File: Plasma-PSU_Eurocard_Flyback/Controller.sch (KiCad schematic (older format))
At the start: 4 parts

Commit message: Block diagram, Connectivity, Isolation
- First page reservered for block diagram
- Connectors moved to separate sheet
- Opto-isolators for signal inputs on HV board
- Fuse added to SMPS
- Pinheader for Arduino pin-out, UART, I2C, SPI
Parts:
- removed J?: I2C, symbol Connector_Generic:Conn_01x02
- removed SW?: SW_RESET, symbol Switch:SW_Push
- added J?: Arduino_Pinout_01-15, symbol Connector_Generic:Conn_01x15
- added J?: Arduino_Pinout_16-30, symbol Connector_Generic:Conn_01x15
- added J?: SPI, symbol Connector_Generic:Conn_01x06
- added J?: I2C, symbol Connector_Generic:Conn_02x04_Odd_Even
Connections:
- net labels added: D13_16, RES_3
- wire segments 14 -> 84
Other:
- note added: "I2C\n\nSCL\nSDA\n+5V\nGND"
- note added: "SPI\n\nSCK\nMISO\nMOSI\nCS\n+5V\nGND"
- note removed: "SDA\nSCL"
- moved on the sheet: J?

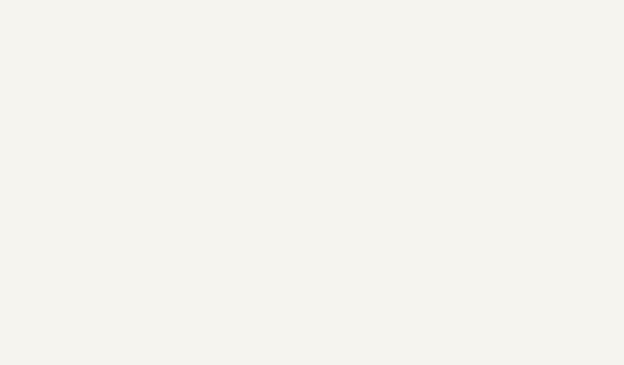
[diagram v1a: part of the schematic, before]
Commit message: STM6600 power-up included
An STM6600 IC is now used to enable stand-by and touch-button operation
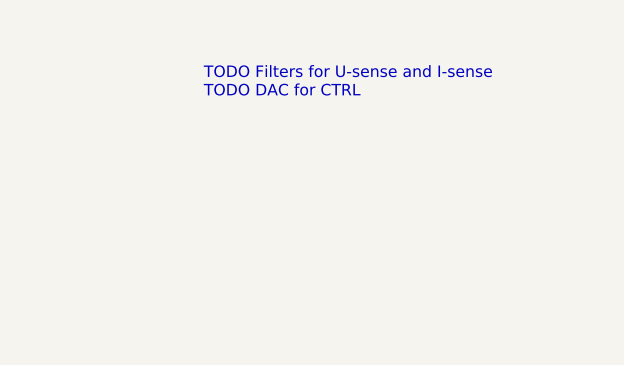
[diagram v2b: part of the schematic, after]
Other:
- note added: "TODO Filters for U-sense and I-sense\nTODO DAC for CTRL"
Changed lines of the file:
@@
 	4150 3500 4150 4400
 Connection ~ 4900 3500
+Text Notes 9000 1000 0    50   ~ 0
+TODO Filters for U-sense and I-sense\nTODO DAC for CTRL
 $EndSCHEMATC

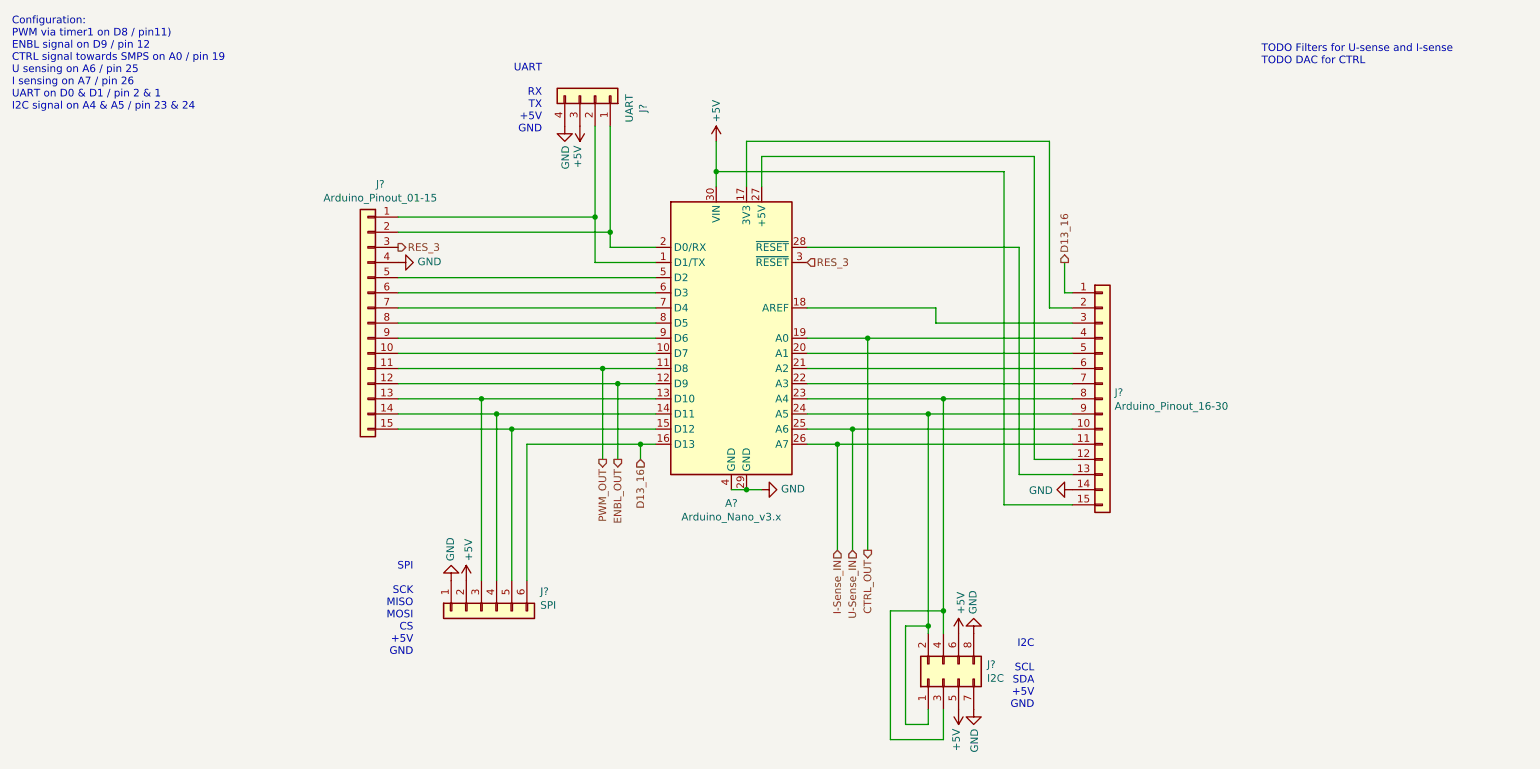
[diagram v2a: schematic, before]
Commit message: Filters for sense signals
- RC filters on U-sense and I-sense included
- Block diagram refined
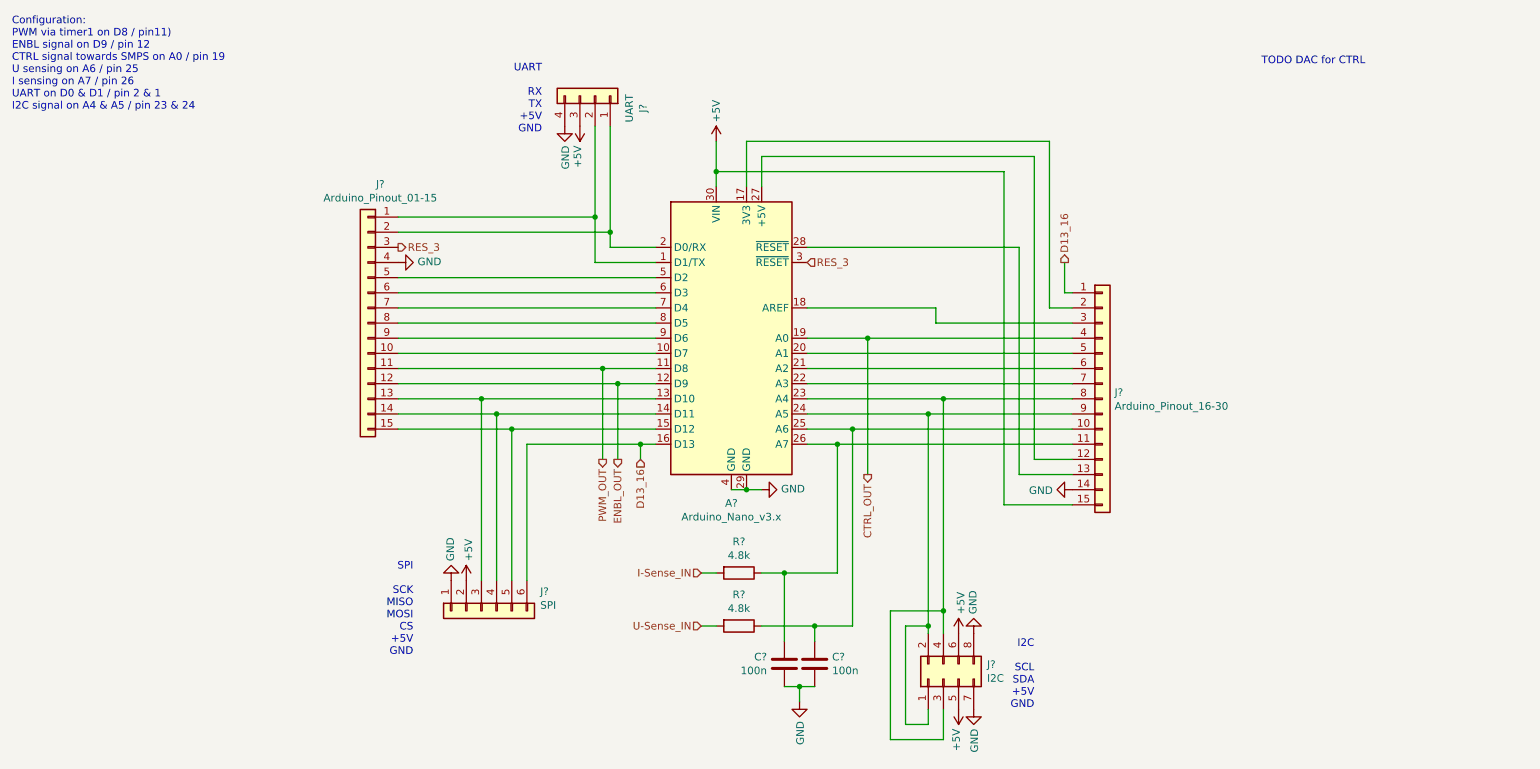
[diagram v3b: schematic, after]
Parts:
- added C? (x2): 100n, symbol Device:C
- added R? (x2): 4.8k, symbol Device:R
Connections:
- net GND: now also C?.1, C?.2
- net I-Sense_IN: now also R?.2; no longer A?.26 (A7), J?.11 (Pin_11)
- net U-Sense_IN: now also R?.2; no longer A?.25 (A6), J?.10 (Pin_10)
- new net: A?.25 (A6), C?.1, J?.10 (Pin_10), R?.1
- new net: A?.26 (A7), C?.2, J?.11 (Pin_11), R?.1
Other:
- note added: "TODO DAC for CTRL"
- note removed: "TODO Filters for U-sense and I-sense\nTODO DAC for CTRL"
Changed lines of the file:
@@
 Sheet 3 5
 Title "Plasma-PSU_Eurocard_Flyback"
-Date "2020-04-07"
-Rev "0.0.3"
+Date "2020-04-08"
+Rev "0.0.4"
 Comp "University of Ljubljana"
 Comment1 "Biotechnical faculty"
@@
 	1    0    0    -1
 $EndComp
-Text HLabel 6400 4200 3    50   Output ~ 0
+Text HLabel 6400 3700 3    50   Output ~ 0
 CTRL_OUT
 Text HLabel 4750 3600 3    50   Output ~ 0
 ENBL_OUT
-Text HLabel 6200 4200 3    50   Input ~ 0
+Text HLabel 5300 4350 0    50   Input ~ 0
 I-Sense_IN
 Text HLabel 4650 3600 3    50   Output ~ 0
 PWM_OUT
-Text HLabel 6300 4200 3    50   Input ~ 0
+Text HLabel 5300 4700 0    50   Input ~ 0
 U-Sense_IN
 $Comp
@@
 $EndComp
 Wire Wire Line
-	6200 4200 6200 3500
-Wire Wire Line
 	6000 3500 6200 3500
 Wire Wire Line
-	6300 4200 6300 3400
-Wire Wire Line
 	6000 3400 6300 3400
-Wire Wire Line
-	6400 4200 6400 2800
 Wire Wire Line
 	6000 2800 6400 2800
@@
 Connection ~ 4900 3500
 Text Notes 9000 1000 0    50   ~ 0
-TODO Filters for U-sense and I-sense\nTODO DAC for CTRL
+TODO DAC for CTRL
+Wire Wire Line
+	6400 3700 6400 2800
+$Comp
+L Device:R R?
+U 1 1 5E90D904
+P 5550 4350
+F 0 "R?" V 5343 4350 50  0000 C CNN
+F 1 "4.8k" V 5434 4350 50  0000 C CNN
+F 2 "" V 5480 4350 50  0001 C CNN
+F 3 "~" H 5550 4350 50  0001 C CNN
+	1    5550 4350
+	0    1    1    0
+$EndComp
+$Comp
+L Device:R R?
+U 1 1 5E90DE41
+P 5550 4700
+F 0 "R?" V 5343 4700 50  0000 C CNN
+F 1 "4.8k" V 5434 4700 50  0000 C CNN
+F 2 "" V 5480 4700 50  0001 C CNN
+F 3 "~" H 5550 4700 50  0001 C CNN
+	1    5550 4700
+	0    1    1    0
+$EndComp
+Wire Wire Line
+	5400 4350 5300 4350
+Wire Wire Line
+	5300 4700 5400 4700
+Wire Wire Line
+	6200 3500 6200 4350
+Wire Wire Line
+	6300 3400 6300 4700
+$Comp
+L Device:C C?
+U 1 1 5E9180BC
+P 5850 4950
+F 0 "C?" H 5735 4904 50  0000 R CNN
+F 1 "100n" H 5735 4995 50  0000 R CNN
+F 2 "" H 5888 4800 50  0001 C CNN
+F 3 "~" H 5850 4950 50  0001 C CNN
+	1    5850 4950
+	1    0    0    1
+$EndComp
+$Comp
+L Device:C C?
+U 1 1 5E9189A9
+P 6050 4950
+F 0 "C?" H 6165 4996 50  0000 L CNN
+F 1 "100n" H 6165 4905 50  0000 L CNN
+F 2 "" H 6088 4800 50  0001 C CNN
+F 3 "~" H 6050 4950 50  0001 C CNN
+	1    6050 4950
+	1    0    0    -1
+$EndComp
+Wire Wire Line
+	5700 4700 6050 4700
+Wire Wire Line
+	5700 4350 5850 4350
+Wire Wire Line
+	5850 4800 5850 4350
+Wire Wire Line
+	6050 4800 6050 4700
+$Comp
+L power:GND #PWR?
+U 1 1 5E92882A
+P 5950 5200
+F 0 "#PWR?" H 5950 4950 50  0001 C CNN
+F 1 "GND" V 5955 5072 50  0000 R CNN
+F 2 "" H 5950 5200 50  0001 C CNN
+F 3 "" H 5950 5200 50  0001 C CNN
+	1    5950 5200
+	1    0    0    -1
+$EndComp
+Wire Wire Line
+	5850 5100 5950 5100
+Wire Wire Line
+	5950 5200 5950 5100
+Connection ~ 5950 5100
+Wire Wire Line
+	5950 5100 6050 5100
+Connection ~ 5850 4350
+Connection ~ 6050 4700
+Wire Wire Line
+	5850 4350 6200 4350
+Wire Wire Line
+	6050 4700 6300 4700
 $EndSCHEMATC

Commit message: DAC sets U_out
DAC converter in SMPS sheet sets boost modules output voltage.
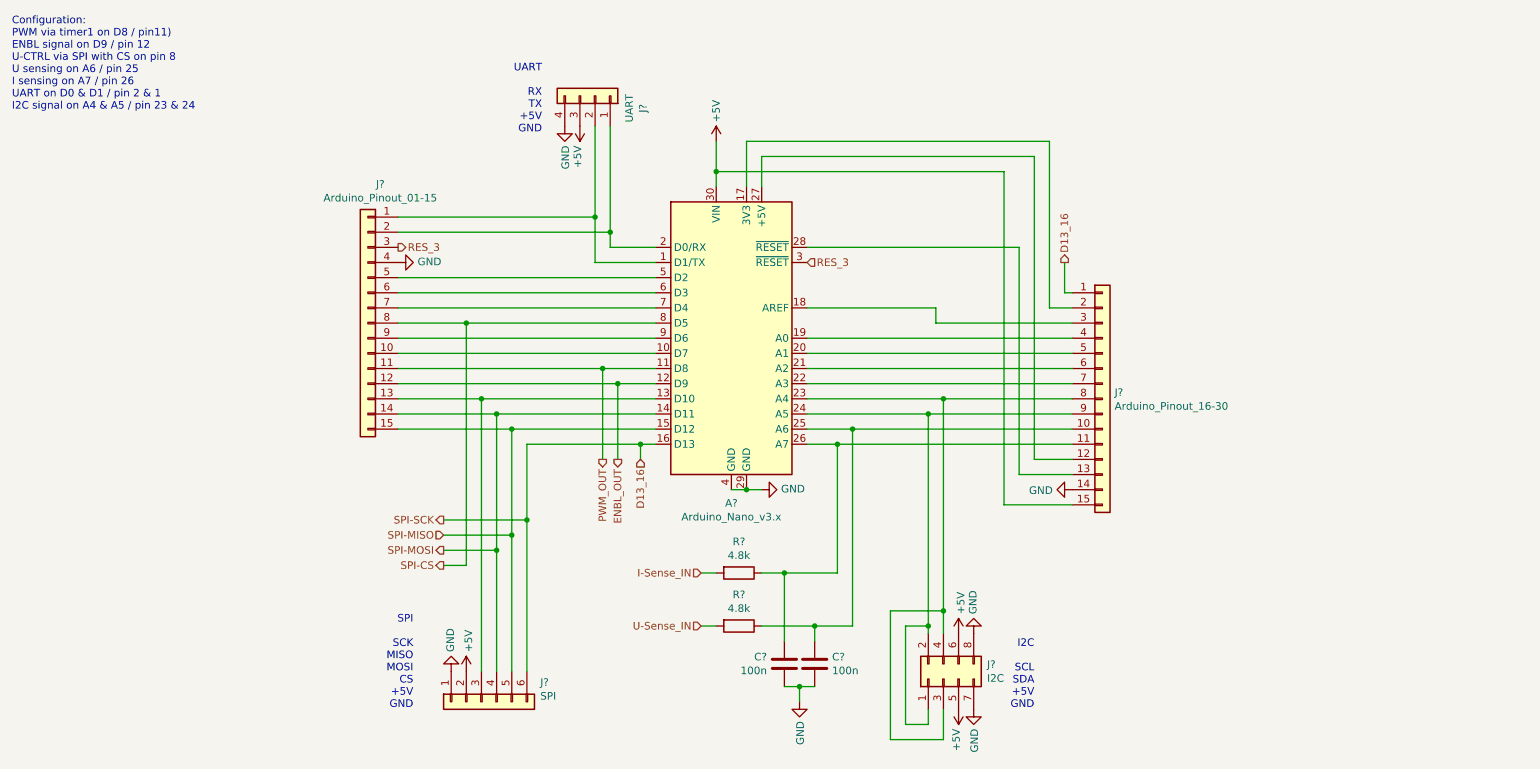
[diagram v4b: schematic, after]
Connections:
- net SPI-MOSI: now reaches A?.14 (D11), J?.14 (Pin_14), J?.4 (Pin_4)
- net SPI-MISO: now reaches A?.15 (D12), J?.15 (Pin_15), J?.5 (Pin_5)
- net SPI-CS: now reaches A?.8 (D5), J?.8 (Pin_8)
- net CTRL_OUT: no longer names the net of A?.19 (A0), J?.4 (Pin_4)
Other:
- note added: "Configuration:\nPWM via timer1 on D8 / pin11)\nENBL signal on D9 / pin 12\nU-CTRL via SPI with CS on pin 8\nU sensing on A6 / pin 25\nI sensing on A7 / pin 26\nUART on D0 & D1 / pin 2 & 1\nI2C signal on A4 & A5 / pin 23 & 24"
- note removed: "Configuration:\nPWM via timer1 on D8 / pin11)\nENBL signal on D9 / pin 12\nCTRL signal towards SMPS on A0 / pin 19\nU sensing on A6 / pin 25\nI sensing on A7 / pin 26\nUART on D0 & D1 / pin 2 & 1\nI2C signal on A4 & A5 / pin 23 & 24"
- note removed: "TODO DAC for CTRL"
- moved on the sheet: J?
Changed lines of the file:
@@
 	1    0    0    -1
 $EndComp
-Text HLabel 6400 3700 3    50   Output ~ 0
-CTRL_OUT
 Text HLabel 4750 3600 3    50   Output ~ 0
 ENBL_OUT
@@
 	5600 3800 5500 3800
 Text Notes 750  1300 0    50   ~ 0
-Configuration:\nPWM via timer1 on D8 / pin11)\nENBL signal on D9 / pin 12\nCTRL signal towards SMPS on A0 / pin 19\nU sensing on A6 / pin 25\nI sensing on A7 / pin 26\nUART on D0 & D1 / pin 2 & 1\nI2C signal on A4 & A5 / pin 23 & 24
+Configuration:\nPWM via timer1 on D8 / pin11)\nENBL signal on D9 / pin 12\nU-CTRL via SPI with CS on pin 8\nU sensing on A6 / pin 25\nI sensing on A7 / pin 26\nUART on D0 & D1 / pin 2 & 1\nI2C signal on A4 & A5 / pin 23 & 24
 $Comp
 L Connector_Generic:Conn_01x04 J?
@@
 Wire Wire Line
 	6000 3400 6300 3400
-Wire Wire Line
-	6000 2800 6400 2800
 Text HLabel 4900 3600 3    50   Input ~ 0
 D13_16
@@
 Wire Wire Line
 	6000 3000 7750 3000
-Wire Wire Line
-	6400 2800 7750 2800
-Connection ~ 6400 2800
 Wire Wire Line
 	6850 2700 7750 2700
@@
 Wire Wire Line
 	7500 1600 7500 3600
-$Comp
-L Connector_Generic:Conn_01x06 J?
-U 1 1 5EA74613
-P 3850 4600
-F 0 "J?" V 3722 4212 50  0000 R CNN
-F 1 "SPI" V 3813 4212 50  0000 R CNN
-F 2 "" H 3850 4600 50  0001 C CNN
-F 3 "~" H 3850 4600 50  0001 C CNN
-	1    3850 4600
-	0    -1   1    0
-$EndComp
 Wire Wire Line
 	4700 1400 4700 2100
@@
 	3300 2600 5000 2600
 Wire Wire Line
-	3300 2700 5000 2700
-Wire Wire Line
 	3300 2800 5000 2800
 Wire Wire Line
@@
 	3300 3100 4750 3100
 Connection ~ 4750 3100
-Wire Wire Line
-	3300 3200 3850 3200
-$Comp
-L power:GND #PWR?
-U 1 1 5EA92261
-P 3650 4400
-F 0 "#PWR?" H 3650 4150 50  0001 C CNN
-F 1 "GND" V 3655 4272 50  0000 R CNN
-F 2 "" H 3650 4400 50  0001 C CNN
-F 3 "" H 3650 4400 50  0001 C CNN
-	1    3650 4400
-	-1   0    0    1
-$EndComp
-$Comp
-L power:+5V #PWR?
-U 1 1 5EA927CA
-P 3750 4400
-F 0 "#PWR?" H 3750 4250 50  0001 C CNN
-F 1 "+5V" V 3765 4528 50  0000 L CNN
-F 2 "" H 3750 4400 50  0001 C CNN
-F 3 "" H 3750 4400 50  0001 C CNN
-	1    3750 4400
-	1    0    0    -1
-$EndComp
 Text Notes 7500 5250 2    50   ~ 0
 I2C\n\nSCL\nSDA\n+5V\nGND
@@
 	1    0    0    -1
 $EndComp
-Text Notes 3400 4900 2    50   ~ 0
-SPI\n\nSCK\nMISO\nMOSI\nCS\n+5V\nGND
-Wire Wire Line
-	3850 4400 3850 3200
-Connection ~ 3850 3200
-Wire Wire Line
-	3850 3200 5000 3200
-Wire Wire Line
-	3300 3400 4050 3400
-Wire Wire Line
-	3300 3300 3950 3300
-Wire Wire Line
-	3950 4400 3950 3300
-Connection ~ 3950 3300
-Wire Wire Line
-	3950 3300 5000 3300
-Wire Wire Line
-	4050 4400 4050 3400
-Connection ~ 4050 3400
-Wire Wire Line
-	4050 3400 5000 3400
-Wire Wire Line
-	4900 3500 4150 3500
-Wire Wire Line
-	4150 3500 4150 4400
 Connection ~ 4900 3500
-Text Notes 9000 1000 0    50   ~ 0
-TODO DAC for CTRL
-Wire Wire Line
-	6400 3700 6400 2800
 $Comp
 L Device:R R?
@@
 Wire Wire Line
 	6050 4700 6300 4700
+Wire Wire Line
+	4900 3500 4150 3500
+Connection ~ 4050 3400
+Connection ~ 3950 3300
+Wire Wire Line
+	3950 3300 5000 3300
+Wire Wire Line
+	3300 3300 3950 3300
+Wire Wire Line
+	4050 3400 5000 3400
+Wire Wire Line
+	3300 3400 4050 3400
+Connection ~ 3850 3200
+Wire Wire Line
+	3850 3200 5000 3200
+Wire Wire Line
+	3300 3200 3850 3200
+Text Notes 3400 5250 2    50   ~ 0
+SPI\n\nSCK\nMISO\nMOSI\nCS\n+5V\nGND
+$Comp
+L power:+5V #PWR?
+U 1 1 5EA927CA
+P 3750 5000
+F 0 "#PWR?" H 3750 4850 50  0001 C CNN
+F 1 "+5V" V 3765 5128 50  0000 L CNN
+F 2 "" H 3750 5000 50  0001 C CNN
+F 3 "" H 3750 5000 50  0001 C CNN
+	1    3750 5000
+	1    0    0    -1
+$EndComp
+$Comp
+L power:GND #PWR?
+U 1 1 5EA92261
+P 3650 5000
+F 0 "#PWR?" H 3650 4750 50  0001 C CNN
+F 1 "GND" V 3655 4872 50  0000 R CNN
+F 2 "" H 3650 5000 50  0001 C CNN
+F 3 "" H 3650 5000 50  0001 C CNN
+	1    3650 5000
+	-1   0    0    1
+$EndComp
+$Comp
+L Connector_Generic:Conn_01x06 J?
+U 1 1 5EA74613
+P 3850 5200
+F 0 "J?" V 3722 4812 50  0000 R CNN
+F 1 "SPI" V 3813 4812 50  0000 R CNN
+F 2 "" H 3850 5200 50  0001 C CNN
+F 3 "~" H 3850 5200 50  0001 C CNN
+	1    3850 5200
+	0    -1   1    0
+$EndComp
+Wire Wire Line
+	4150 3500 4150 4000
+Wire Wire Line
+	4050 3400 4050 4100
+Connection ~ 4150 4000
+Wire Wire Line
+	4150 4000 4150 5000
+Wire Wire Line
+	3600 4000 4150 4000
+Wire Wire Line
+	3950 3300 3950 4200
+Text HLabel 3600 4000 0    50   Output ~ 0
+SPI-SCK
+Text HLabel 3600 4100 0    50   Input ~ 0
+SPI-MISO
+Text HLabel 3600 4200 0    50   Output ~ 0
+SPI-MOSI
+Text HLabel 3600 4300 0    50   Output ~ 0
+SPI-CS
+Wire Wire Line
+	3850 3200 3850 5000
+Wire Wire Line
+	3300 2700 3750 2700
+Wire Wire Line
+	3750 2700 3750 4300
+Wire Wire Line
+	3750 4300 3600 4300
+Connection ~ 3750 2700
+Wire Wire Line
+	3750 2700 5000 2700
+Wire Wire Line
+	4050 4100 3600 4100
+Connection ~ 4050 4100
+Wire Wire Line
+	4050 4100 4050 5000
+Wire Wire Line
+	3600 4200 3950 4200
+Connection ~ 3950 4200
+Wire Wire Line
+	3950 4200 3950 5000
+Wire Wire Line
+	6000 2800 7750 2800
 $EndSCHEMATC
